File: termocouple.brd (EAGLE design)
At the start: 69.8 x 100 mm, 19 parts, among them IC1 MAX6675, IC2 MAX6675, IC3 MAX6675, IC4 MAX6675, U2 TC1262_VDB, X2 1751248, X3 1751248, X4 1751248, X5 1751248

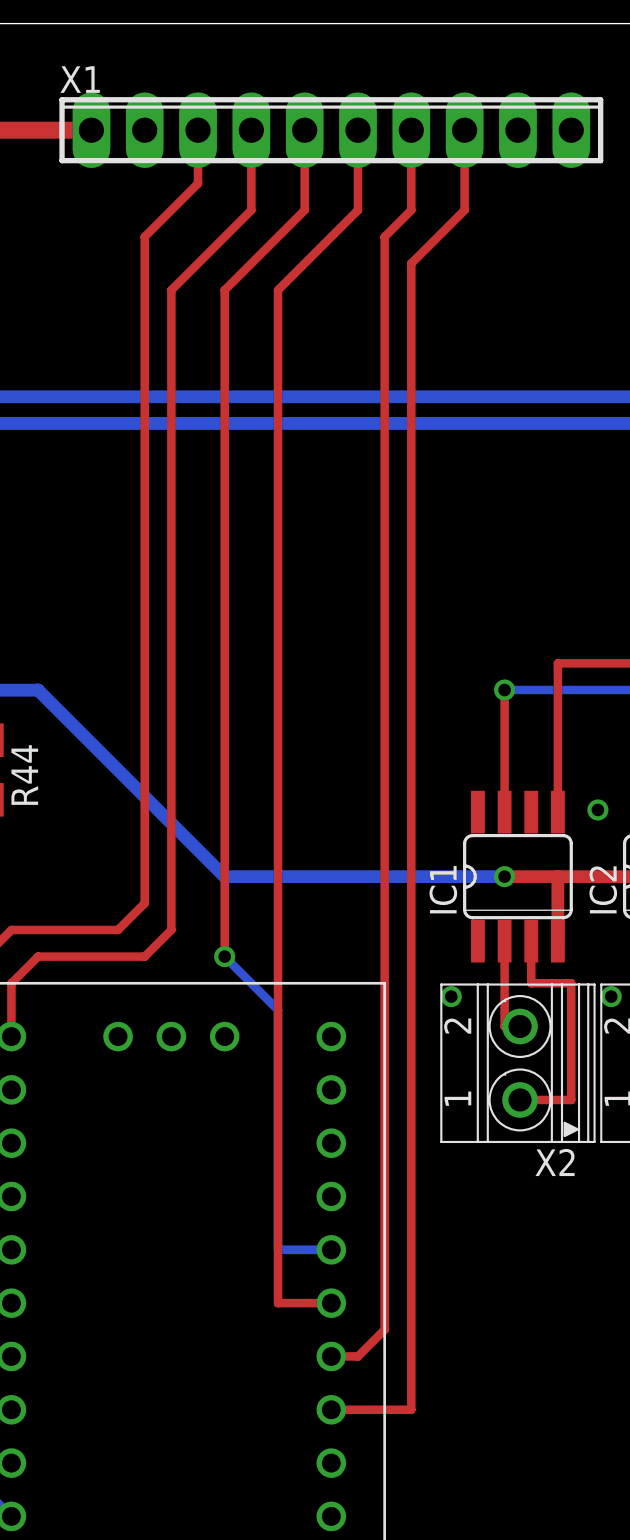
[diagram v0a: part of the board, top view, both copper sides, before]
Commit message: wiring change
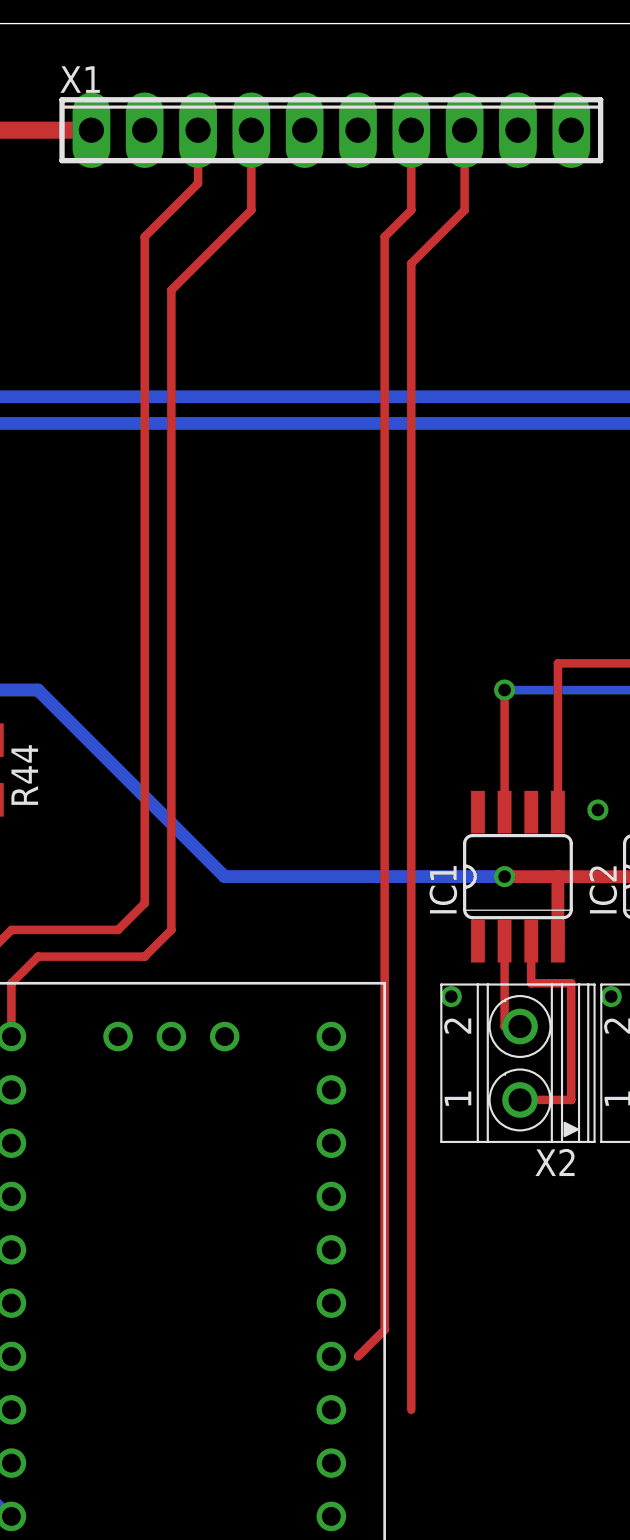
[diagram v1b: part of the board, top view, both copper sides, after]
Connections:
- removed net N$11: U$1.D11, X1.6
- removed net N$12: U$1.D12, X1.5
- new net N$24: X1.6
- new net N$25: X1.5
- net N$1: now also U$1.D7; no longer U$1.D3
- net N$10: no longer U$1.D10
- net N$2: now also U$1.D8; no longer U$1.D4
- net N$3: now also U$1.D10; no longer U$1.D6
- net N$4: now also U$1.D9; no longer U$1.D5
- net N$6: now also U$1.D11; no longer U$1.D7
- net N$7: now also U$1.D12; no longer U$1.D8
- net N$9: no longer U$1.D9
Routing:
- net N$11: track 60.0 -> 0.00 mm
- net N$12: track 58.5 -> 0.00 mm, vias 1 -> 0
- net N$9: track 65.8 -> 62.0 mm
- net N$10: track 60.7 -> 59.5 mm
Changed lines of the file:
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@@
 <contactref element="IC2" pad="7"/>
 <contactref element="IC3" pad="7"/>
-<contactref element="U$1" pad="D3"/>
 <wire x1="62.865" y1="55.1434" x2="62.865" y2="60.96" width="0.4064" layer="1"/>
 <wire x1="62.865" y1="60.96" x2="62.23" y2="60.96" width="0.4064" layer="1"/>
@@
 <via x="40.005" y="60.96" extent="1-16" drill="0.6" shape="square"/>
 <wire x1="40.005" y1="60.96" x2="47.625" y2="60.96" width="0.4064" layer="16"/>
-<wire x1="31.75" y1="11.43" x2="40.005" y2="55.1434" width="0" layer="19" extent="1-1"/>
+<contactref element="U$1" pad="D7"/>
+<wire x1="31.75" y1="21.59" x2="40.005" y2="55.1434" width="0" layer="19" extent="1-1"/>
 </signal>
 <signal name="N$2">
@@
 <contactref element="IC3" pad="5"/>
 <contactref element="IC2" pad="5"/>
-<contactref element="U$1" pad="D4"/>
 <wire x1="65.405" y1="55.1434" x2="65.405" y2="62.23" width="0.4064" layer="1"/>
 <wire x1="65.405" y1="62.23" x2="57.785" y2="62.23" width="0.4064" layer="1"/>
@@
 <contactref element="IC1" pad="5"/>
 <wire x1="42.545" y1="55.1434" x2="42.545" y2="62.23" width="0.4064" layer="1"/>
-<wire x1="31.75" y1="13.97" x2="42.545" y2="55.1434" width="0" layer="19" extent="1-1"/>
+<contactref element="U$1" pad="D8"/>
+<wire x1="31.75" y1="24.13" x2="42.545" y2="55.1434" width="0" layer="19" extent="1-1"/>
 </signal>
 <signal name="+3V3">
@@
 <signal name="N$4">
 <contactref element="IC1" pad="6"/>
-<contactref element="U$1" pad="D5"/>
-<wire x1="31.75" y1="16.51" x2="41.275" y2="55.1434" width="0" layer="19" extent="1-1"/>
+<contactref element="U$1" pad="D9"/>
+<wire x1="31.75" y1="26.67" x2="41.275" y2="55.1434" width="0" layer="19" extent="1-1"/>
 </signal>
 <signal name="N$6">
 <contactref element="IC3" pad="6"/>
-<contactref element="U$1" pad="D7"/>
-<wire x1="31.75" y1="21.59" x2="56.515" y2="55.1434" width="0" layer="19" extent="1-1"/>
-</signal>
-<signal name="N$3">
-<contactref element="IC2" pad="6"/>
-<contactref element="U$1" pad="D6"/>
-<wire x1="31.75" y1="19.05" x2="48.895" y2="55.1434" width="0" layer="19" extent="1-1"/>
+<contactref element="U$1" pad="D11"/>
+<wire x1="31.75" y1="31.75" x2="56.515" y2="55.1434" width="0" layer="19" extent="1-1"/>
 </signal>
 <signal name="N$7">
 <contactref element="IC4" pad="6"/>
-<contactref element="U$1" pad="D8"/>
-<wire x1="31.75" y1="24.13" x2="64.135" y2="55.1434" width="0" layer="19" extent="1-1"/>
+<contactref element="U$1" pad="D12"/>
+<wire x1="31.75" y1="34.29" x2="64.135" y2="55.1434" width="0" layer="19" extent="1-1"/>
 </signal>
 <signal name="+12V">
@@
 </signal>
 <signal name="N$9">
-<contactref element="U$1" pad="D9"/>
 <contactref element="X1" pad="8"/>
-<wire x1="31.75" y1="26.67" x2="35.56" y2="26.67" width="0.4064" layer="1"/>
 <wire x1="35.56" y1="26.67" x2="35.56" y2="81.28" width="0.4064" layer="1"/>
 <wire x1="35.56" y1="81.28" x2="38.1" y2="83.82" width="0.4064" layer="1"/>
@@
 </signal>
 <signal name="N$10">
-<contactref element="U$1" pad="D10"/>
 <contactref element="X1" pad="7"/>
-<wire x1="31.75" y1="29.21" x2="33.02" y2="29.21" width="0.4064" layer="1"/>
 <wire x1="33.02" y1="29.21" x2="34.29" y2="30.48" width="0.4064" layer="1"/>
 <wire x1="34.29" y1="30.48" x2="34.29" y2="82.55" width="0.4064" layer="1"/>
 <wire x1="34.29" y1="82.55" x2="35.56" y2="83.82" width="0.4064" layer="1"/>
 <wire x1="35.56" y1="83.82" x2="35.56" y2="87.63" width="0.4064" layer="1"/>
-</signal>
-<signal name="N$11">
-<contactref element="U$1" pad="D11"/>
-<contactref element="X1" pad="6"/>
-<wire x1="31.75" y1="31.75" x2="29.21" y2="31.75" width="0.4064" layer="1"/>
-<wire x1="29.21" y1="31.75" x2="29.21" y2="80.01" width="0.4064" layer="1"/>
-<wire x1="29.21" y1="80.01" x2="33.02" y2="83.82" width="0.4064" layer="1"/>
-<wire x1="33.02" y1="83.82" x2="33.02" y2="87.63" width="0.4064" layer="1"/>
-</signal>
-<signal name="N$12">
-<contactref element="U$1" pad="D12"/>
-<contactref element="X1" pad="5"/>
-<wire x1="31.75" y1="34.29" x2="29.21" y2="34.29" width="0.4064" layer="16"/>
-<wire x1="29.21" y1="34.29" x2="29.21" y2="45.72" width="0.4064" layer="16"/>
-<wire x1="29.21" y1="45.72" x2="26.67" y2="48.26" width="0.4064" layer="16"/>
-<via x="26.67" y="48.26" extent="1-16" drill="0.6" shape="square"/>
-<wire x1="26.67" y1="48.26" x2="26.67" y2="80.01" width="0.4064" layer="1"/>
-<wire x1="26.67" y1="80.01" x2="30.48" y2="83.82" width="0.4064" layer="1"/>
-<wire x1="30.48" y1="83.82" x2="30.48" y2="87.63" width="0.4064" layer="1"/>
 </signal>
 <signal name="N$13">
@@
 <wire x1="40.005" y1="44.93" x2="40.74" y2="44.93" width="0.4064" layer="1"/>
 </signal>
+<signal name="N$24">
+<contactref element="X1" pad="6"/>
+</signal>
+<signal name="N$25">
+<contactref element="X1" pad="5"/>
+</signal>
+<signal name="N$3">
+<contactref element="U$1" pad="D10"/>
+<contactref element="IC2" pad="6"/>
+<wire x1="31.75" y1="29.21" x2="48.895" y2="55.1434" width="0" layer="19" extent="1-1"/>
+</signal>
 </signals>

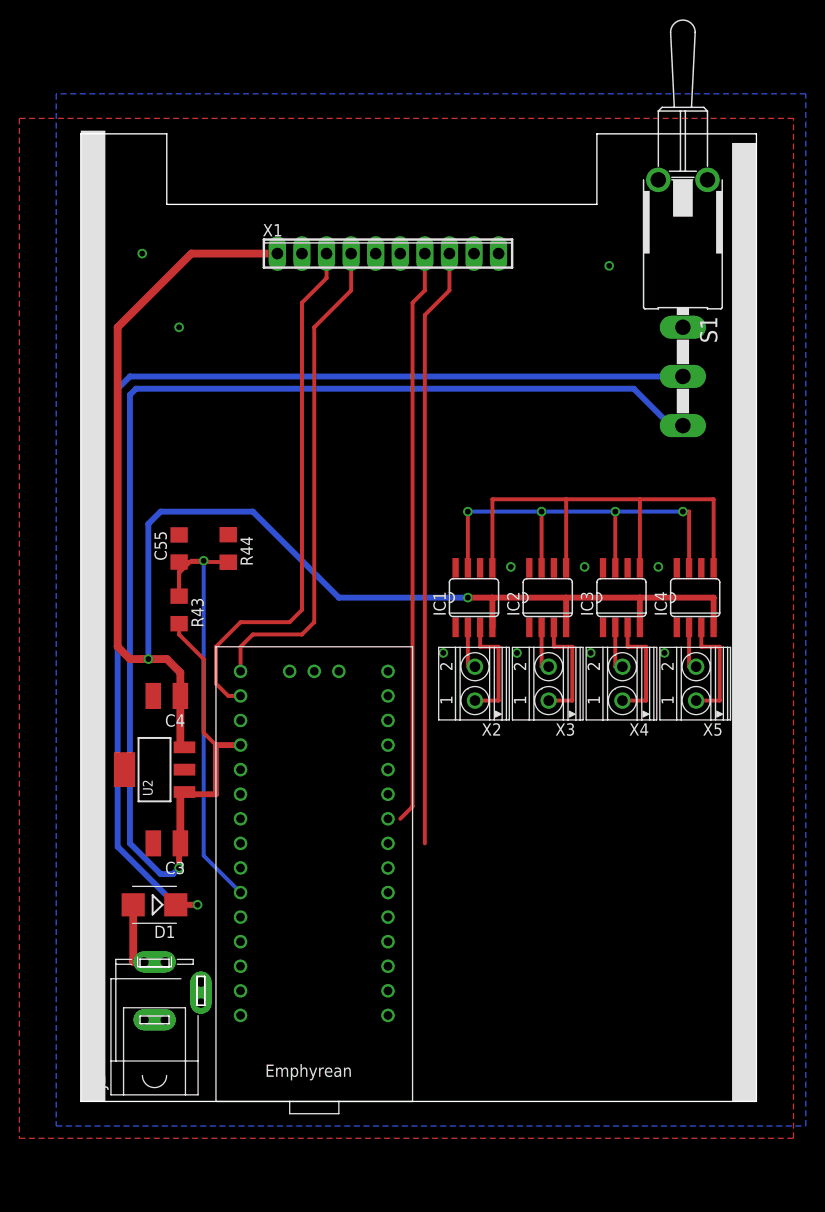
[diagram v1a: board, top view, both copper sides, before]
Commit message: front panel + brd traces
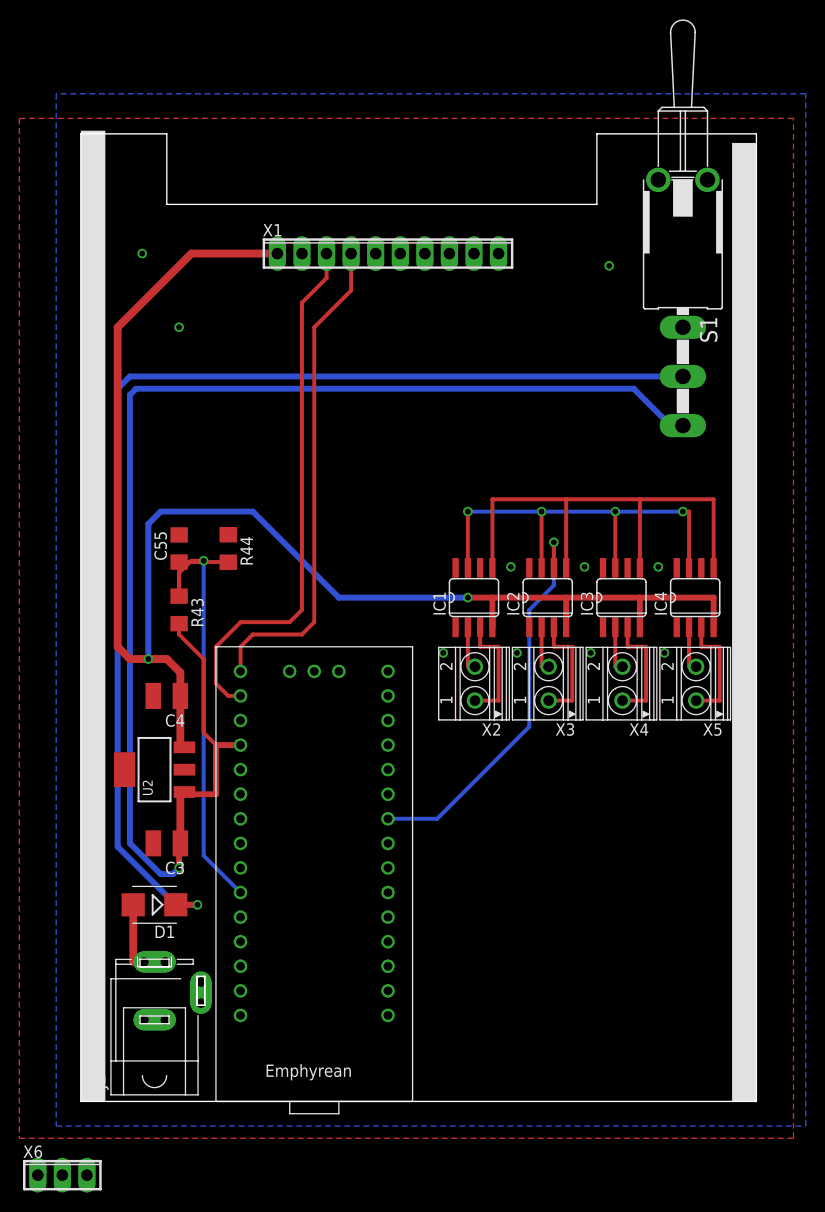
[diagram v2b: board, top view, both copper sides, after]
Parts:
- added X6: (no value), con-phoenix-254:3POL254
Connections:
- removed net N$24: X1.6
- removed net N$25: X1.5
- new net N$11: U$1.D4, X1.7
- new net N$12: U$1.D3, X1.8
- new net N$22: U$1.D0, X6.3
- new net N$23: U$1.D1, X6.2
- net GND: now also X6.1
- net N$10: now also U$1.D5; no longer X1.7
- net N$9: now also U$1.D6, X1.5; no longer X1.8
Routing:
- net N$9: track 62.0 -> 0.00 mm
- net N$10: track 59.5 -> 0.00 mm
- net N$3: track 0.00 -> 41.3 mm, vias 0 -> 1
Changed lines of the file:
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@@
 <attribute name="OC_FARNELL" value="unknown" x="63.5" y="43.18" size="1.778" layer="27" rot="R90" display="off"/>
+</element>
+<element name="X6" library="con-phoenix-254" package="3POL254" value="" x="-1.905" y="-7.62">
+<attribute name="OC_NEWARK" value="unknown" x="-1.905" y="-7.62" size="1.778" layer="27" display="off"/>
+<attribute name="MPN" value="" x="-1.905" y="-7.62" size="1.778" layer="27" display="off"/>
+<attribute name="MF" value="" x="-1.905" y="-7.62" size="1.778" layer="27" display="off"/>
+<attribute name="OC_FARNELL" value="unknown" x="-1.905" y="-7.62" size="1.778" layer="27" display="off"/>
 </element>
 </elements>
@@
 <via x="45.085" y="46.355" extent="1-16" drill="0.6" shape="square"/>
 <via x="37.465" y="46.355" extent="1-16" drill="0.6" shape="square"/>
+<contactref element="X6" pad="1"/>
+<wire x1="6.53435" y1="8.443909375" x2="-4.445" y2="-7.62" width="0" layer="19" extent="1-1"/>
 </signal>
 <signal name="N$4">
@@
 <wire x1="16.51" y1="46.99" x2="16.51" y2="44.45" width="0.4064" layer="1"/>
 </signal>
-<signal name="N$9">
-<contactref element="X1" pad="8"/>
-<wire x1="35.56" y1="26.67" x2="35.56" y2="81.28" width="0.4064" layer="1"/>
-<wire x1="35.56" y1="81.28" x2="38.1" y2="83.82" width="0.4064" layer="1"/>
-<wire x1="38.1" y1="83.82" x2="38.1" y2="87.63" width="0.4064" layer="1"/>
-</signal>
-<signal name="N$10">
-<contactref element="X1" pad="7"/>
-<wire x1="33.02" y1="29.21" x2="34.29" y2="30.48" width="0.4064" layer="1"/>
-<wire x1="34.29" y1="30.48" x2="34.29" y2="82.55" width="0.4064" layer="1"/>
-<wire x1="34.29" y1="82.55" x2="35.56" y2="83.82" width="0.4064" layer="1"/>
-<wire x1="35.56" y1="83.82" x2="35.56" y2="87.63" width="0.4064" layer="1"/>
-</signal>
 <signal name="N$13">
 <contactref element="S1" pad="2"/>
@@
 <wire x1="40.005" y1="44.93" x2="40.74" y2="44.93" width="0.4064" layer="1"/>
 </signal>
-<signal name="N$24">
-<contactref element="X1" pad="6"/>
-</signal>
-<signal name="N$25">
-<contactref element="X1" pad="5"/>
-</signal>
 <signal name="N$3">
 <contactref element="U$1" pad="D10"/>
 <contactref element="IC2" pad="6"/>
-<wire x1="31.75" y1="29.21" x2="48.895" y2="55.1434" width="0" layer="19" extent="1-1"/>
+<wire x1="31.75" y1="29.21" x2="36.83" y2="29.21" width="0.4064" layer="16"/>
+<wire x1="36.83" y1="29.21" x2="46.355" y2="38.735" width="0.4064" layer="16"/>
+<wire x1="46.355" y1="38.735" x2="46.355" y2="50.8" width="0.4064" layer="16"/>
+<wire x1="46.355" y1="50.8" x2="48.895" y2="53.34" width="0.4064" layer="16"/>
+<wire x1="48.895" y1="53.34" x2="48.895" y2="57.785" width="0.4064" layer="16"/>
+<via x="48.895" y="57.785" extent="1-16" drill="0.6" shape="square"/>
+<wire x1="48.895" y1="57.785" x2="48.895" y2="55.1434" width="0.4064" layer="1"/>
+</signal>
+<signal name="N$9">
+<contactref element="U$1" pad="D6"/>
+<contactref element="X1" pad="5"/>
+<wire x1="31.75" y1="19.05" x2="30.48" y2="87.63" width="0" layer="19" extent="1-1"/>
+</signal>
+<signal name="N$10">
+<contactref element="U$1" pad="D5"/>
+</signal>
+<signal name="N$11">
+<contactref element="U$1" pad="D4"/>
+<contactref element="X1" pad="7"/>
+<wire x1="31.75" y1="13.97" x2="35.56" y2="87.63" width="0" layer="19" extent="1-1"/>
+</signal>
+<signal name="N$12">
+<contactref element="U$1" pad="D3"/>
+<contactref element="X1" pad="8"/>
+<wire x1="31.75" y1="11.43" x2="38.1" y2="87.63" width="0" layer="19" extent="1-1"/>
+</signal>
+<signal name="N$22">
+<contactref element="U$1" pad="D0"/>
+<contactref element="X6" pad="3"/>
+<wire x1="0.635" y1="-7.62" x2="16.51" y2="11.43" width="0" layer="19" extent="1-1"/>
+</signal>
+<signal name="N$23">
+<contactref element="U$1" pad="D1"/>
+<contactref element="X6" pad="2"/>
+<wire x1="-1.905" y1="-7.62" x2="16.51" y2="8.89" width="0" layer="19" extent="1-1"/>
 </signal>
 </signals>
